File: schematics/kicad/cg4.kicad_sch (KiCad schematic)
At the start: 0 parts

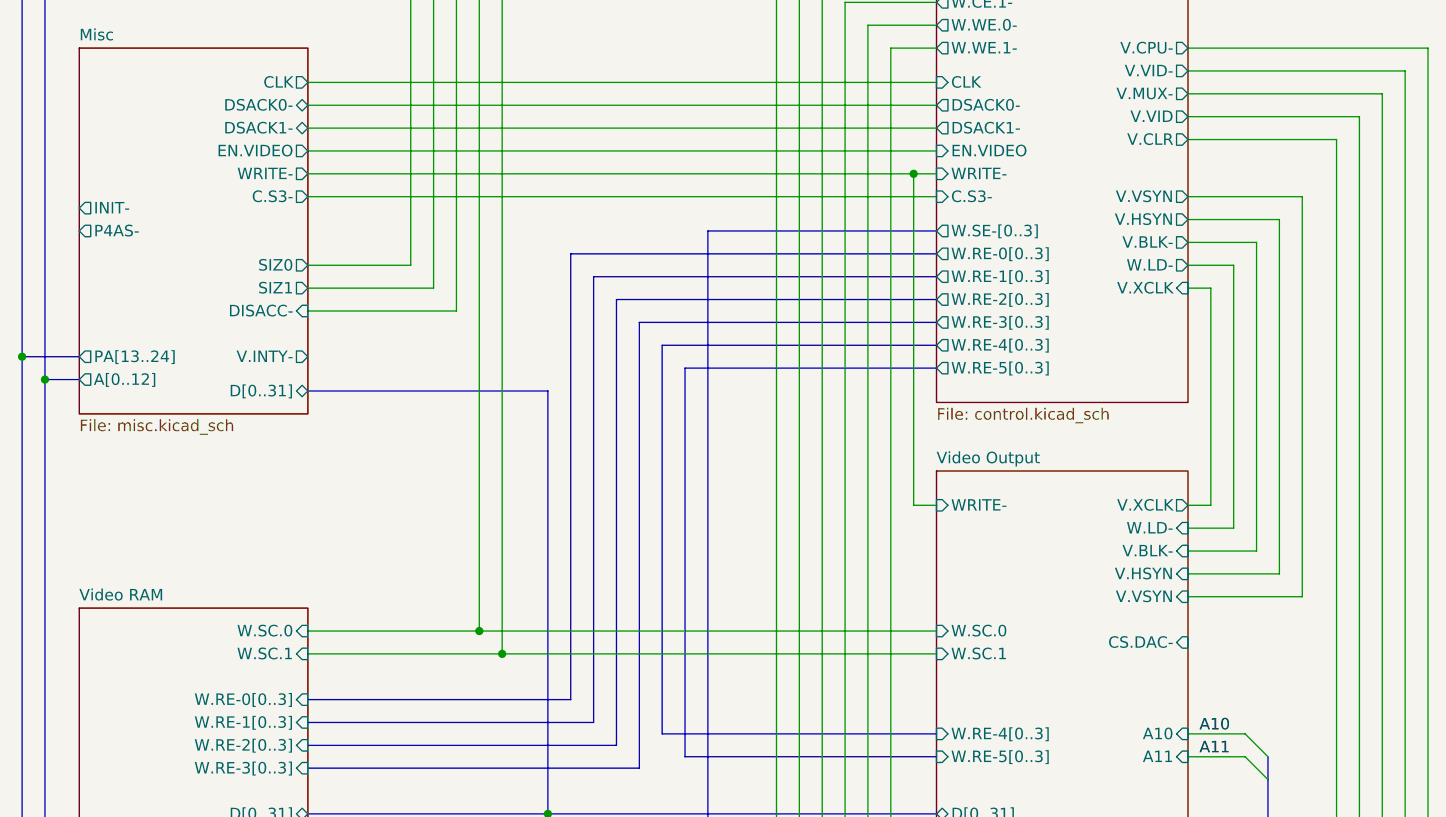
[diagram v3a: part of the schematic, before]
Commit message: Fix layout of the memory chips based on the board Fix the orientation of the P4 connector Connect CS.DAC- based on the board Change the orientation of the ECL resistors to route better Fix the copper islands to match the board, only DAC is on analog island, ECL and crystal are separate. Fix ECL VCC to VCC Confirm VEE not used Add PALs - U1000 missing
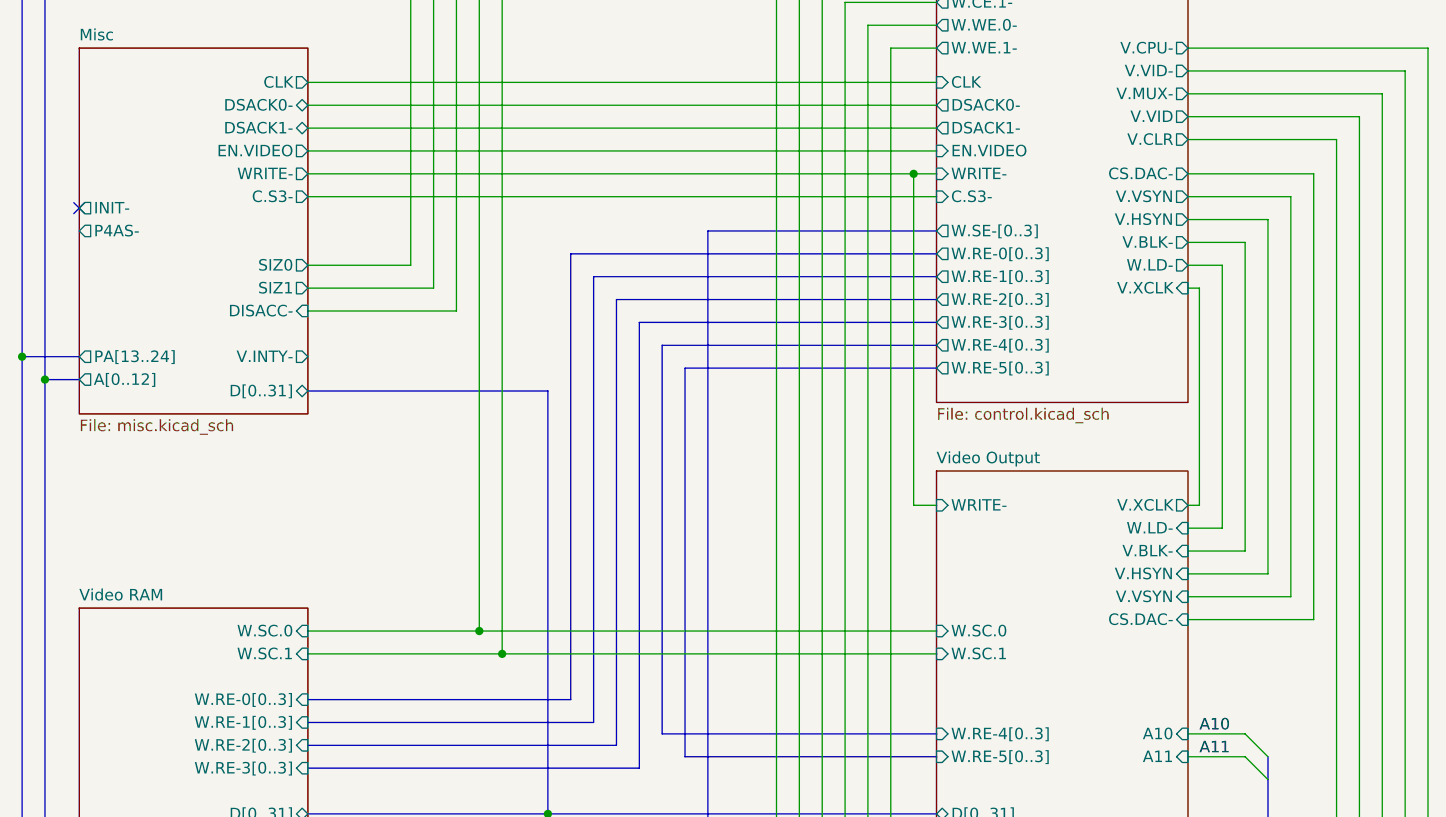
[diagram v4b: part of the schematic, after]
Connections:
- no-connect marks 0 -> 1
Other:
- sheet Video Control ports: added CS.DAC-; removed none
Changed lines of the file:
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@@
 		(color 0 0 0 0)
+	)
+	(no_connect
+		(at 43.18 68.58)
 	)
 	(bus_entry
@@
 	(wire
 		(pts
-			(xy 166.37 104.14) (xy 171.45 104.14)
+			(xy 166.37 104.14) (xy 170.18 104.14)
 		)
 		(stroke
@@
 	(wire
 		(pts
-			(xy 166.37 74.93) (xy 171.45 74.93)
-		)
-		(stroke
-			(width 0)
-			(type default)
-		)
-	)
-	(wire
-		(pts
-			(xy 176.53 109.22) (xy 166.37 109.22)
-		)
-		(stroke
-			(width 0)
-			(type default)
-		)
-	)
-	(wire
-		(pts
-			(xy 166.37 101.6) (xy 168.91 101.6)
+			(xy 166.37 74.93) (xy 170.18 74.93)
+		)
+		(stroke
+			(width 0)
+			(type default)
+		)
+	)
+	(wire
+		(pts
+			(xy 175.26 109.22) (xy 166.37 109.22)
+		)
+		(stroke
+			(width 0)
+			(type default)
+		)
+	)
+	(wire
+		(pts
+			(xy 166.37 101.6) (xy 167.64 101.6)
 		)
 		(stroke
@@
 	(wire
 		(pts
+			(xy 180.34 114.3) (xy 166.37 114.3)
+		)
+		(stroke
+			(width 0)
+			(type default)
+		)
+	)
+	(wire
+		(pts
 			(xy 166.37 43.18) (xy 186.69 43.18)
 		)
@@
 	(wire
 		(pts
-			(xy 168.91 77.47) (xy 168.91 101.6)
+			(xy 167.64 77.47) (xy 167.64 101.6)
 		)
 		(stroke
@@
 	(wire
 		(pts
-			(xy 176.53 69.85) (xy 176.53 109.22)
+			(xy 175.26 69.85) (xy 175.26 109.22)
 		)
 		(stroke
@@
 	(wire
 		(pts
-			(xy 166.37 72.39) (xy 173.99 72.39)
+			(xy 166.37 72.39) (xy 172.72 72.39)
 		)
 		(stroke
@@
 	(wire
 		(pts
-			(xy 166.37 69.85) (xy 176.53 69.85)
+			(xy 180.34 64.77) (xy 180.34 114.3)
+		)
+		(stroke
+			(width 0)
+			(type default)
+		)
+	)
+	(wire
+		(pts
+			(xy 166.37 69.85) (xy 175.26 69.85)
 		)
 		(stroke
@@
 		)
 	)
+	(wire
+		(pts
+			(xy 166.37 64.77) (xy 180.34 64.77)
+		)
+		(stroke
+			(width 0)
+			(type default)
+		)
+	)
 	(bus
 		(pts
@@
 	(wire
 		(pts
-			(xy 166.37 106.68) (xy 173.99 106.68)
+			(xy 166.37 106.68) (xy 172.72 106.68)
 		)
 		(stroke
@@
 	(wire
 		(pts
-			(xy 179.07 67.31) (xy 179.07 111.76)
+			(xy 177.8 67.31) (xy 177.8 111.76)
 		)
 		(stroke
@@
 	(wire
 		(pts
-			(xy 166.37 77.47) (xy 168.91 77.47)
+			(xy 166.37 77.47) (xy 167.64 77.47)
 		)
 		(stroke
@@
 	(wire
 		(pts
-			(xy 171.45 74.93) (xy 171.45 104.14)
+			(xy 170.18 74.93) (xy 170.18 104.14)
 		)
 		(stroke
@@
 	(wire
 		(pts
-			(xy 173.99 72.39) (xy 173.99 106.68)
+			(xy 172.72 72.39) (xy 172.72 106.68)
 		)
 		(stroke
@@
 	(wire
 		(pts
-			(xy 166.37 67.31) (xy 179.07 67.31)
+			(xy 166.37 67.31) (xy 177.8 67.31)
 		)
 		(stroke
@@
 	(wire
 		(pts
-			(xy 179.07 111.76) (xy 166.37 111.76)
+			(xy 177.8 111.76) (xy 166.37 111.76)
 		)
 		(stroke
@@
 			)
 		)
+		(pin "CS.DAC-" output
+			(at 166.37 64.77 0)
+			(effects
+				(font
+					(size 1.27 1.27)
+				)
+				(justify right)
+			)
+		)
 		(instances
 			(project "cg4"
@@
 		)
 		(pin "CS.DAC-" input
-			(at 166.37 116.84 0)
-			(effects
-				(font
+			(at 166.37 114.3 0)
+			(effects
+				(font

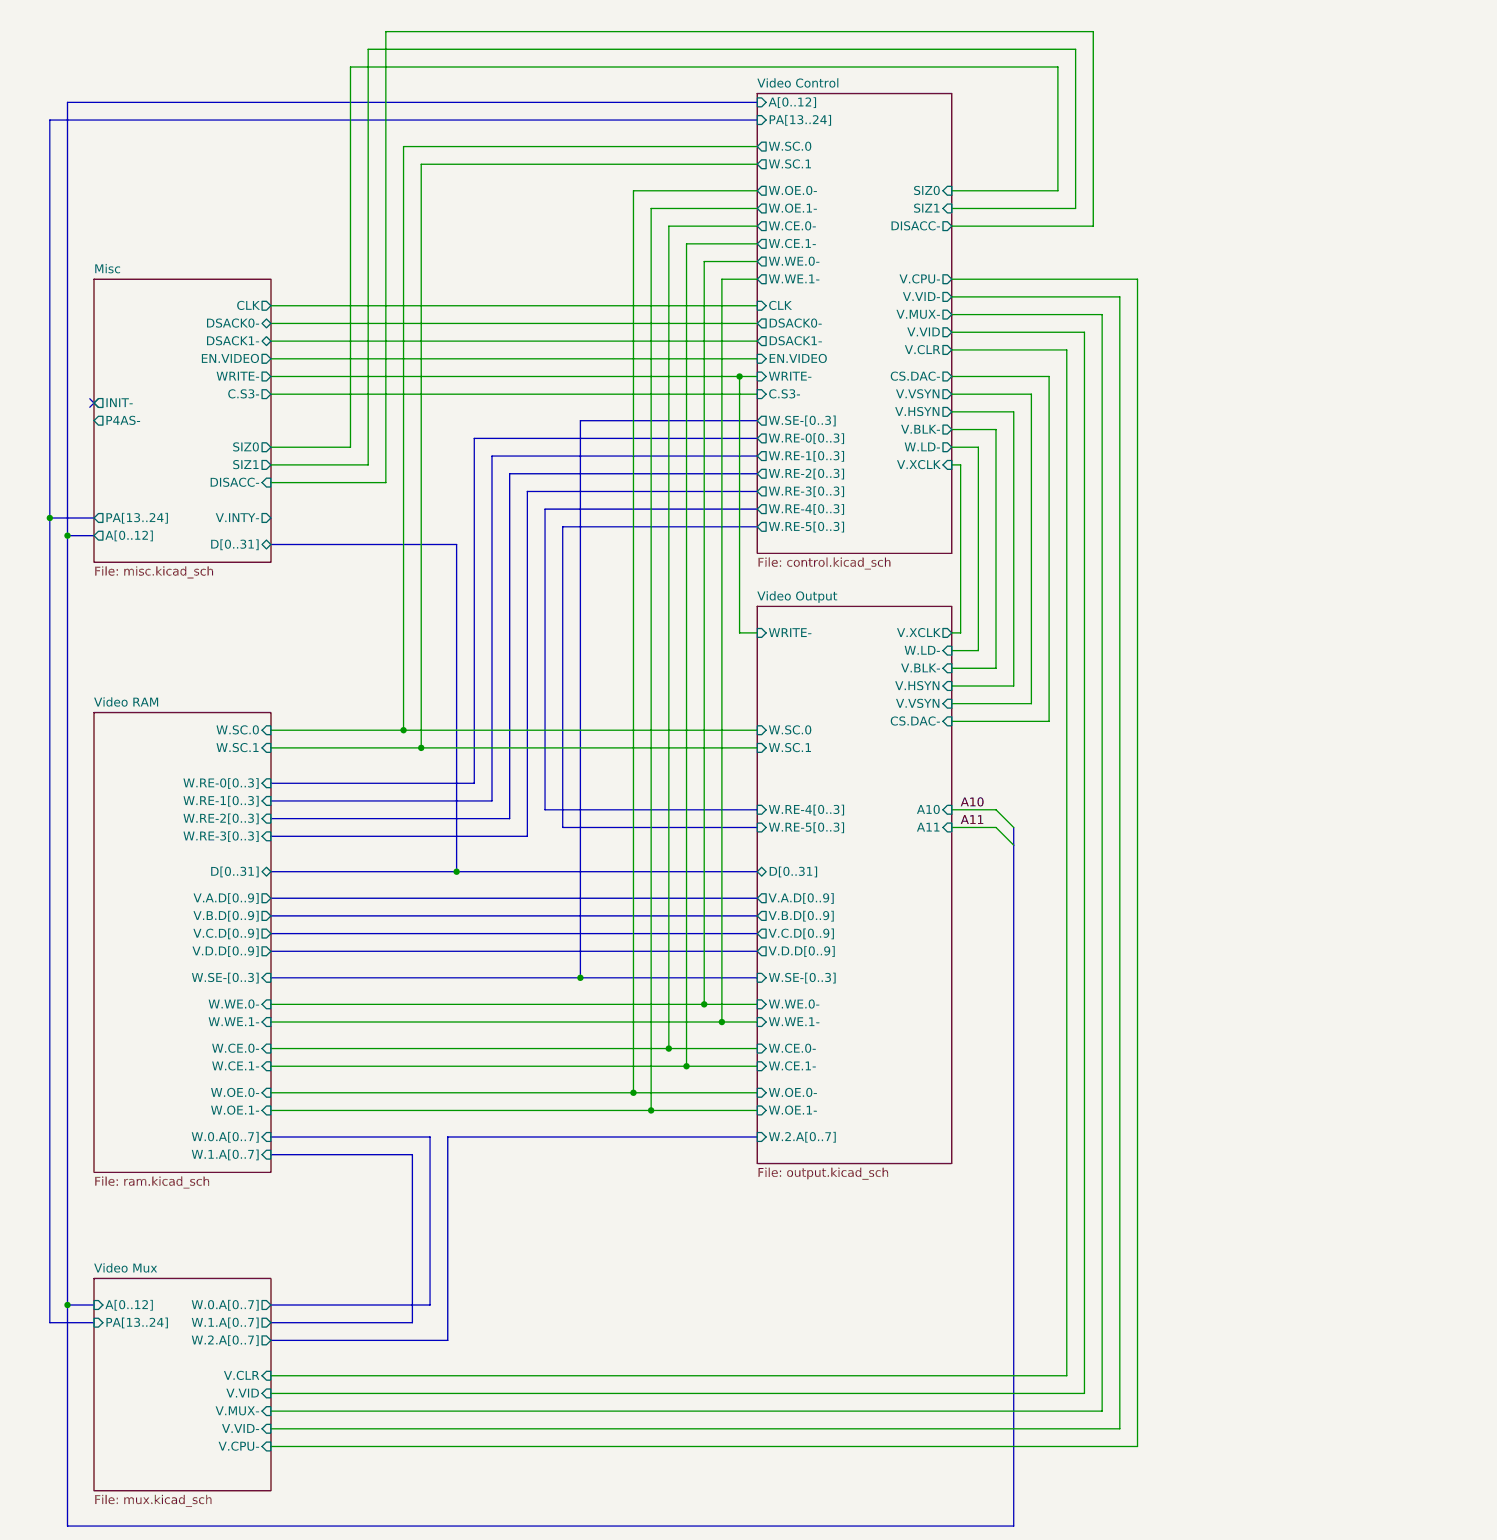
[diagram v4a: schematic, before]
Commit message: Fix the schematics as per the tracing of the actual board. fork a layout with the original positioning. New version PCB that should make routing easier.
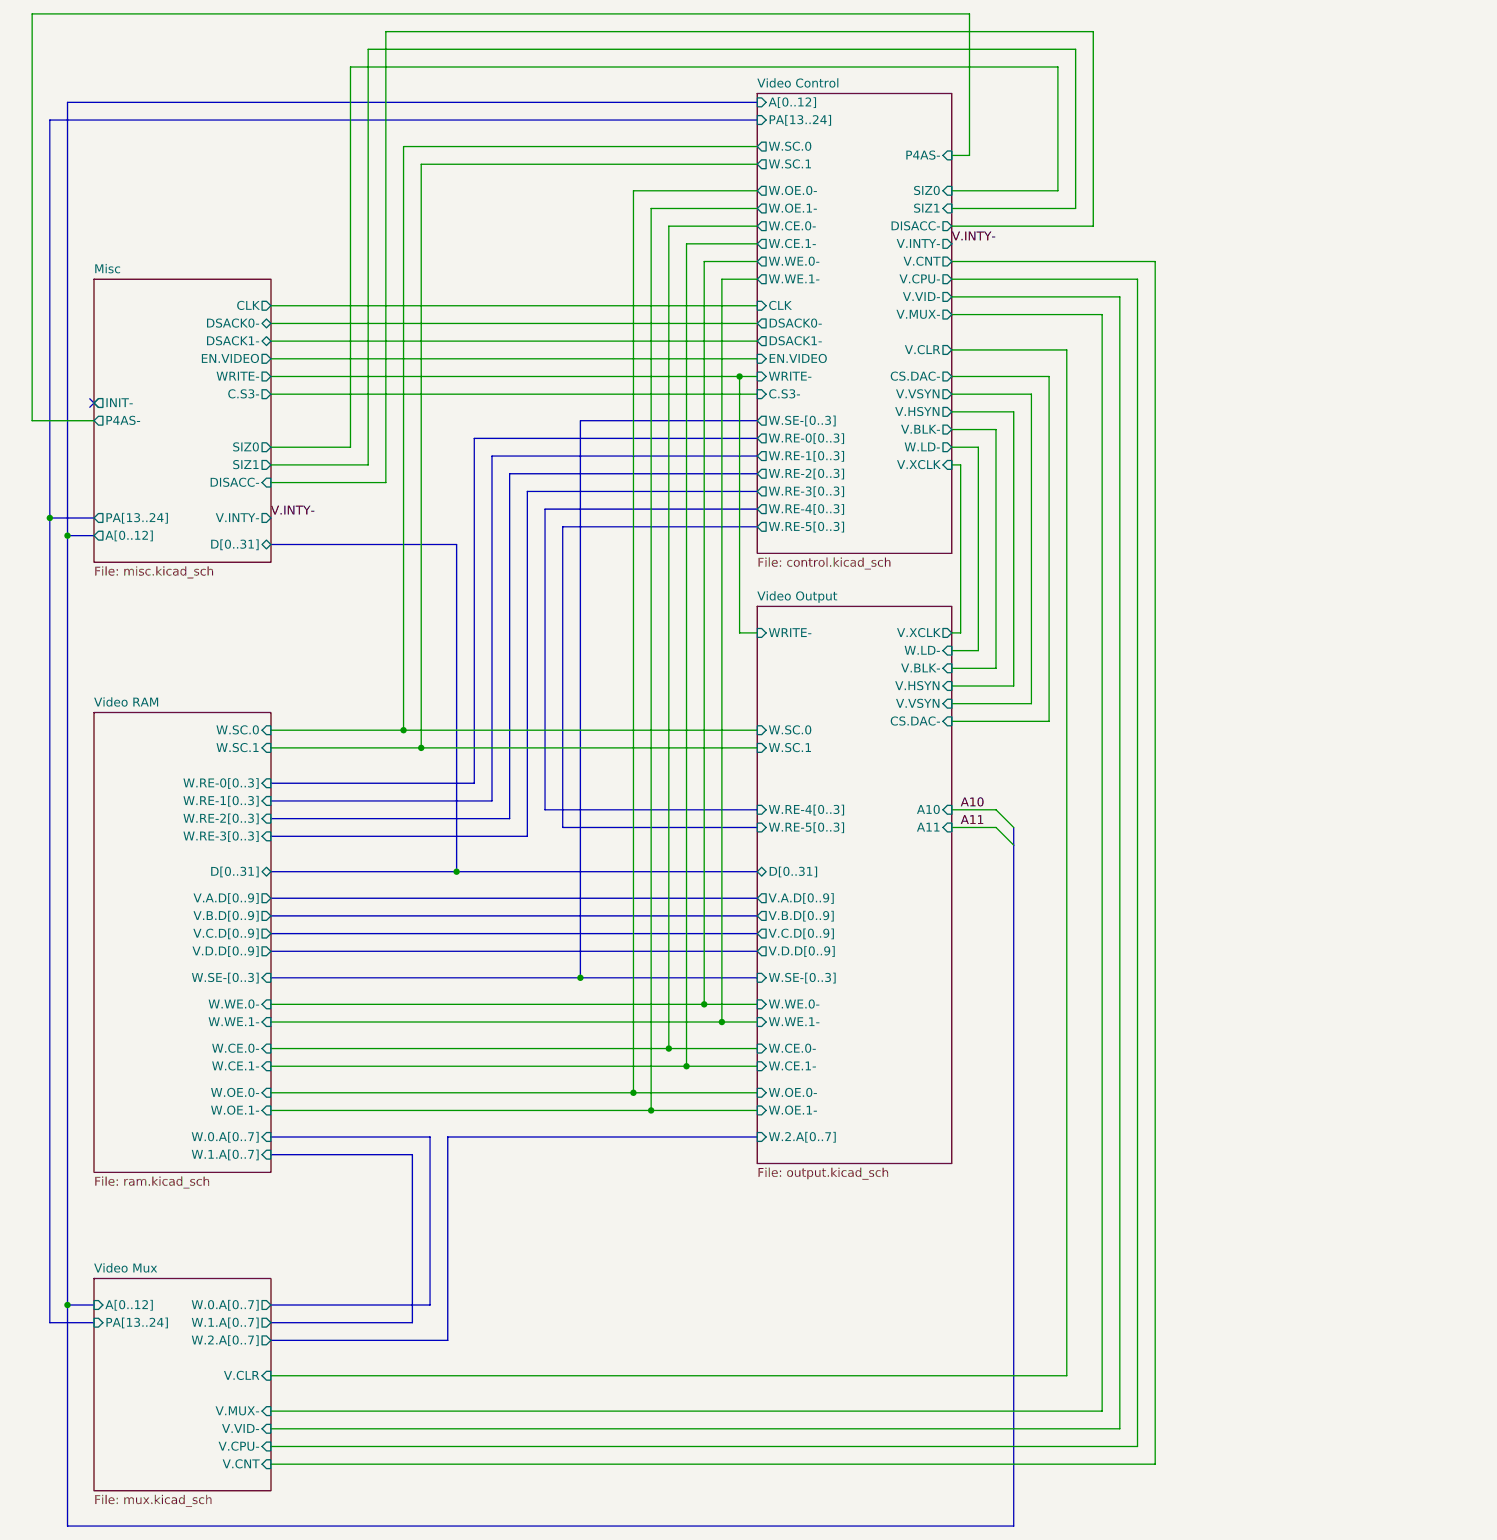
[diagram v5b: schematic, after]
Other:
- sheet Video Control ports: added P4AS-, V.CNT, V.INTY-; removed V.VID
- sheet Video Mux ports: added V.CNT; removed V.VID
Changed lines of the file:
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@@
+	(wire
+		(pts
+			(xy 195.58 48.26) (xy 195.58 220.98)
+		)
+		(stroke
+			(width 0)
+			(type default)
+		)
+	)
 	(wire
 		(pts
@@
 		)
 	)
+	(wire
+		(pts
+			(xy 168.91 12.7) (xy 34.29 12.7)
+		)
+		(stroke
+			(width 0)
+			(type default)
+		)
+	)
 	(bus
 		(pts
@@
 		)
 	)
+	(wire
+		(pts
+			(xy 166.37 33.02) (xy 168.91 33.02)
+		)
+		(stroke
+			(width 0)
+			(type default)
+		)
+	)
 	(bus
 		(pts
@@
 	(wire
 		(pts
+			(xy 34.29 12.7) (xy 34.29 71.12)
+		)
+		(stroke
+			(width 0)
+			(type default)
+		)
+	)
+	(wire
+		(pts
 			(xy 133.35 157.48) (xy 138.43 157.48)
 		)
@@
 	(wire
 		(pts
+			(xy 166.37 48.26) (xy 195.58 48.26)
+		)
+		(stroke
+			(width 0)
+			(type default)
+		)
+	)
+	(wire
+		(pts
 			(xy 85.09 80.01) (xy 85.09 15.24)
 		)
@@
 	(wire
 		(pts
+			(xy 34.29 71.12) (xy 43.18 71.12)
+		)
+		(stroke
+			(width 0)
+			(type default)
+		)
+	)
+	(wire
+		(pts
 			(xy 177.8 67.31) (xy 177.8 111.76)
 		)
@@
 		)
 	)
+	(wire
+		(pts
+			(xy 68.58 220.98) (xy 195.58 220.98)
+		)
+		(stroke
+			(width 0)
+			(type default)
+		)
+	)
 	(bus
 		(pts
@@
 	(wire
 		(pts
-			(xy 185.42 210.82) (xy 68.58 210.82)
-		)
-		(stroke
-			(width 0)
-			(type default)
-		)
-	)
-	(wire
-		(pts
 			(xy 68.58 218.44) (xy 193.04 218.44)
 		)
@@
 	(wire
 		(pts
-			(xy 166.37 58.42) (xy 185.42 58.42)
-		)
-		(stroke
-			(width 0)
-			(type default)
-		)
-	)
-	(wire
-		(pts
 			(xy 68.58 57.15) (xy 138.43 57.15)
 		)
@@
 	(wire
 		(pts
-			(xy 185.42 58.42) (xy 185.42 210.82)
-		)
-		(stroke
-			(width 0)
-			(type default)
-		)
-	)
-	(wire
-		(pts
 			(xy 130.81 48.26) (xy 130.81 154.94)
 		)
@@
 	(wire
 		(pts
+			(xy 168.91 33.02) (xy 168.91 12.7)
+		)
+		(stroke
+			(width 0)
+			(type default)
+		)
+	)
+	(wire
+		(pts
 			(xy 135.89 101.6) (xy 138.43 101.6)
 		)
@@
 			(width 0)
 			(type default)
+		)
+	)
+	(label "V.INTY-"
+		(at 166.37 45.72 0)
+		(effects
+			(font
+				(size 1.27 1.27)
+			)
+			(justify left bottom)
 		)
 	)
@@
 	(label "A11"
 		(at 167.64 129.54 0)
+		(effects
+			(font
+				(size 1.27 1.27)
+			)
+			(justify left bottom)
+		)
+	)
+	(label "V.INTY-"
+		(at 68.58 85.09 0)
 		(effects
 			(font
@@
 			)
 		)
-		(pin "V.VID" output
-			(at 166.37 58.42 0)
-			(effects
-				(font
-					(size 1.27 1.27)
-				)
-				(justify right)
-			)
-		)
 		(pin "DISACC-" output
 			(at 166.37 43.18 0)
@@
 		(pin "CS.DAC-" output
 			(at 166.37 64.77 0)
+			(effects
+				(font
+					(size 1.27 1.27)
+				)
+				(justify right)
+			)
+		)
+		(pin "P4AS-" input
+			(at 166.37 33.02 0)
+			(effects
+				(font
+					(size 1.27 1.27)
+				)
+				(justify right)
+			)
+		)
+		(pin "V.CNT" output
+			(at 166.37 48.26 0)
+			(effects
+				(font
+					(size 1.27 1.27)
+				)
+				(justify right)
+			)
+		)
+		(pin "V.INTY-" output
+			(at 166.37 45.72 0)
 			(effects
 				(font
@@
 			)
 		)
-		(pin "V.VID" input
-			(at 68.58 210.82 0)
-			(effects
-				(font
-					(size 1.27 1.27)
-				)
-				(justify right)
-			)
-		)
 		(pin "W.0.A[0..7]" output
 			(at 68.58 198.12 0)
@@
 			)
 		)
+		(pin "V.CNT" input
+			(at 68.58 220.98 0)
+			(effects
+				(font
+					(size 1.27 1.27)
+				)
+				(justify right)
+			)
+		)
